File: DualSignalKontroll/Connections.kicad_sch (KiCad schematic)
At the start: 15 parts, among them J10 Power Out, J11 Buttons and switches, J12 Buttons and switches, J13 Power Out, J14 Buttons and switches, SW2 Switch A, SW3 Switch B, SW4 Select A, SW5 Select B, SW6 Switch A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

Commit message: Started on V2
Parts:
- removed J12: Buttons and switches, symbol Connector:Screw_Terminal_01x10
- SW6: value Switch A -> Switch C
- SW7: value Switch B -> Switch D
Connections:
- net at SW6.1 (A): now also SW7.2 (B)
- net at SW7.1 (A): now also J11.10 (Pin_10)
- net at J11.9 (Pin_9), SW3.1 (A): now also SW6.2 (B)
- removed net +10V: SW6.2 (B), SW7.2 (B)
- now unconnected: J10.3 (Pin_3), J11.8 (Pin_8)
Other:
- note added: "10V"
- note removed: "Alt. 1"
- note removed: "Alt. 2"
- note removed: "Antar at disse bruker boardets 12V power Da skal intern Gnd koples til"
- note removed: "Antar at disse bruker egen 10V/12V power Da skal ikke boardes 10V anvendes, men Gnd koples til"
- moved on the sheet: J10, J11, SW2, SW3

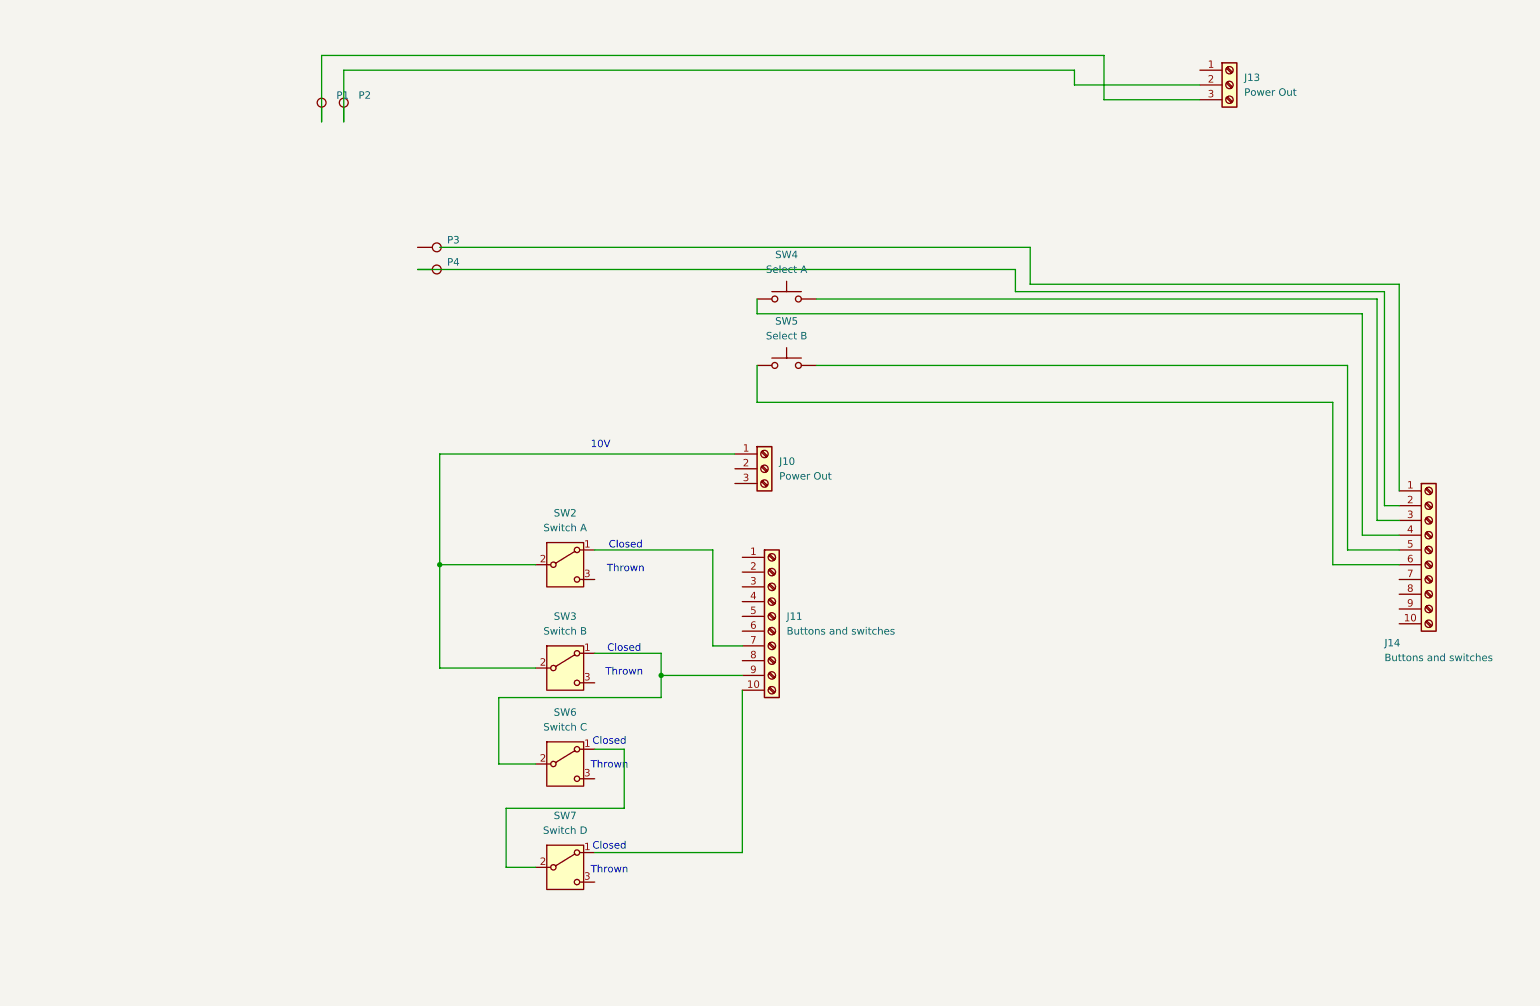
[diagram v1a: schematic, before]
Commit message: Updated schema
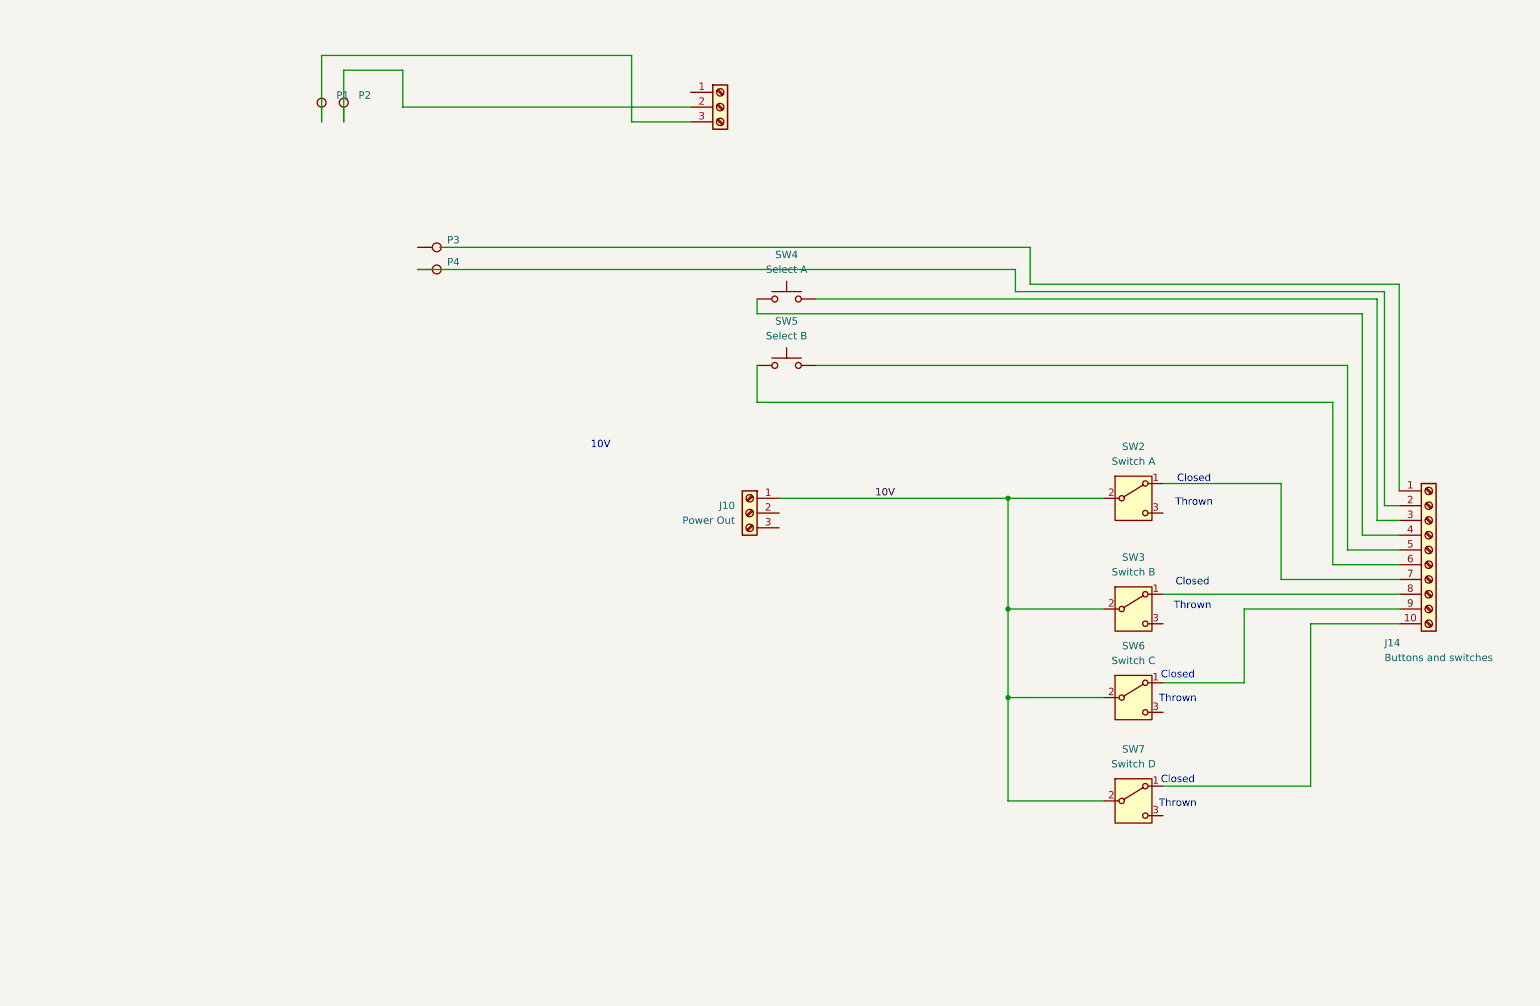
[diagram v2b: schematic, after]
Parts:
- removed J11: Buttons and switches, symbol Connector:Screw_Terminal_01x10
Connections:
- net at J14.10 (Pin_10): now also SW7.1 (A)
- net at J14.7 (Pin_7): now also SW2.1 (A)
- net at J14.8 (Pin_8): now also SW3.1 (A)
- net at J14.9 (Pin_9): now also SW6.1 (A)
- net 10V: now reaches SW6.2 (B)
- net 10V: now also J10.1 (Pin_1), SW2.2 (B), SW3.2 (B), SW7.2 (B); no longer SW3.1 (A)
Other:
- moved on the sheet: J10, SW2, SW3, SW6, SW7

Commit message: Versjon med 4 penser
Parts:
- added P5, P6, P7, P8, P9: ~, symbol Connector:TestPoint
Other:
- note added: "16.1.2026"
- note added: "Alt 1"
- note added: "Alt 2"
- note added: "DCC"
- note added: "Drop 0.3V"
- note added: "Ekstern wiring"
- note added: "Terje Sandstrøm"
- note added: "Track"

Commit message: working with more debug info
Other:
- note removed: "10V"
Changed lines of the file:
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@@
-		)
-	)
-	(text "10V"
-		(exclude_from_sim no)
-		(at 121.666 100.076 0)
-		(effects
-			(font
-				(size 1.27 1.27)
-			)
 		)
 	)
@@
 	)
 	(junction
-		(at 116.84 66.04)
-		(diameter 0)
-		(color 0 0 0 0)
-	)
-	(junction
 		(at 191.77 109.22)
-		(diameter 0)
-		(color 0 0 0 0)
-	)
-	(junction
-		(at 123.19 69.85)
 		(diameter 0)
 		(color 0 0 0 0)
@@
 	(wire
 		(pts
-			(xy 93.98 66.04) (xy 116.84 66.04)
-		)
-		(stroke
-			(width 0)
-			(type default)
-		)
-	)
-	(wire
-		(pts
 			(xy 250.19 118.11) (xy 250.19 86.36)
 		)
@@
 	(wire
 		(pts
-			(xy 195.58 66.04) (xy 195.58 72.39)
-		)
-		(stroke
-			(width 0)
-			(type default)
-		)
-	)
-	(wire
-		(pts
 			(xy 87.63 35.56) (xy 77.47 35.56)
 		)
@@
 	(wire
 		(pts
-			(xy 123.19 69.85) (xy 123.19 152.4)
-		)
-		(stroke
-			(width 0)
-			(type default)
-		)
-	)
-	(wire
-		(pts
 			(xy 259.08 113.03) (xy 255.27 113.03)
 		)
@@
 	(wire
 		(pts
-			(xy 90.17 69.85) (xy 123.19 69.85)
-		)
-		(stroke
-			(width 0)
-			(type default)
-		)
-	)
-	(wire
-		(pts
-			(xy 116.84 66.04) (xy 116.84 138.43)
+			(xy 90.17 69.85) (xy 193.04 69.85)
 		)
 		(stroke
@@
 	(wire
 		(pts
-			(xy 259.08 72.39) (xy 259.08 107.95)
-		)
-		(stroke
-			(width 0)
-			(type default)
-		)
-	)
-	(wire
-		(pts
 			(xy 158.75 86.36) (xy 250.19 86.36)
 		)
@@
 	(wire
 		(pts
-			(xy 116.84 66.04) (xy 195.58 66.04)
-		)
-		(stroke
-			(width 0)
-			(type default)
-		)
-	)
-	(wire
-		(pts
 			(xy 193.04 73.66) (xy 256.54 73.66)
 		)
@@
 	(wire
 		(pts
-			(xy 123.19 69.85) (xy 193.04 69.85)
-		)
-		(stroke
-			(width 0)
-			(type default)
-		)
-	)
-	(wire
-		(pts
 			(xy 238.76 123.19) (xy 259.08 123.19)
 		)
@@
 		)
 		(stroke
-			(width 0)
-			(type default)
-		)
-	)
-	(wire
-		(pts
-			(xy 195.58 72.39) (xy 259.08 72.39)
-		)
-		(stroke
